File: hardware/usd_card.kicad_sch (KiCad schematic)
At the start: 11 parts, among them J3 MicroSD_502570-0893, U10 AP2112K-3.3, U9 TXB0104D

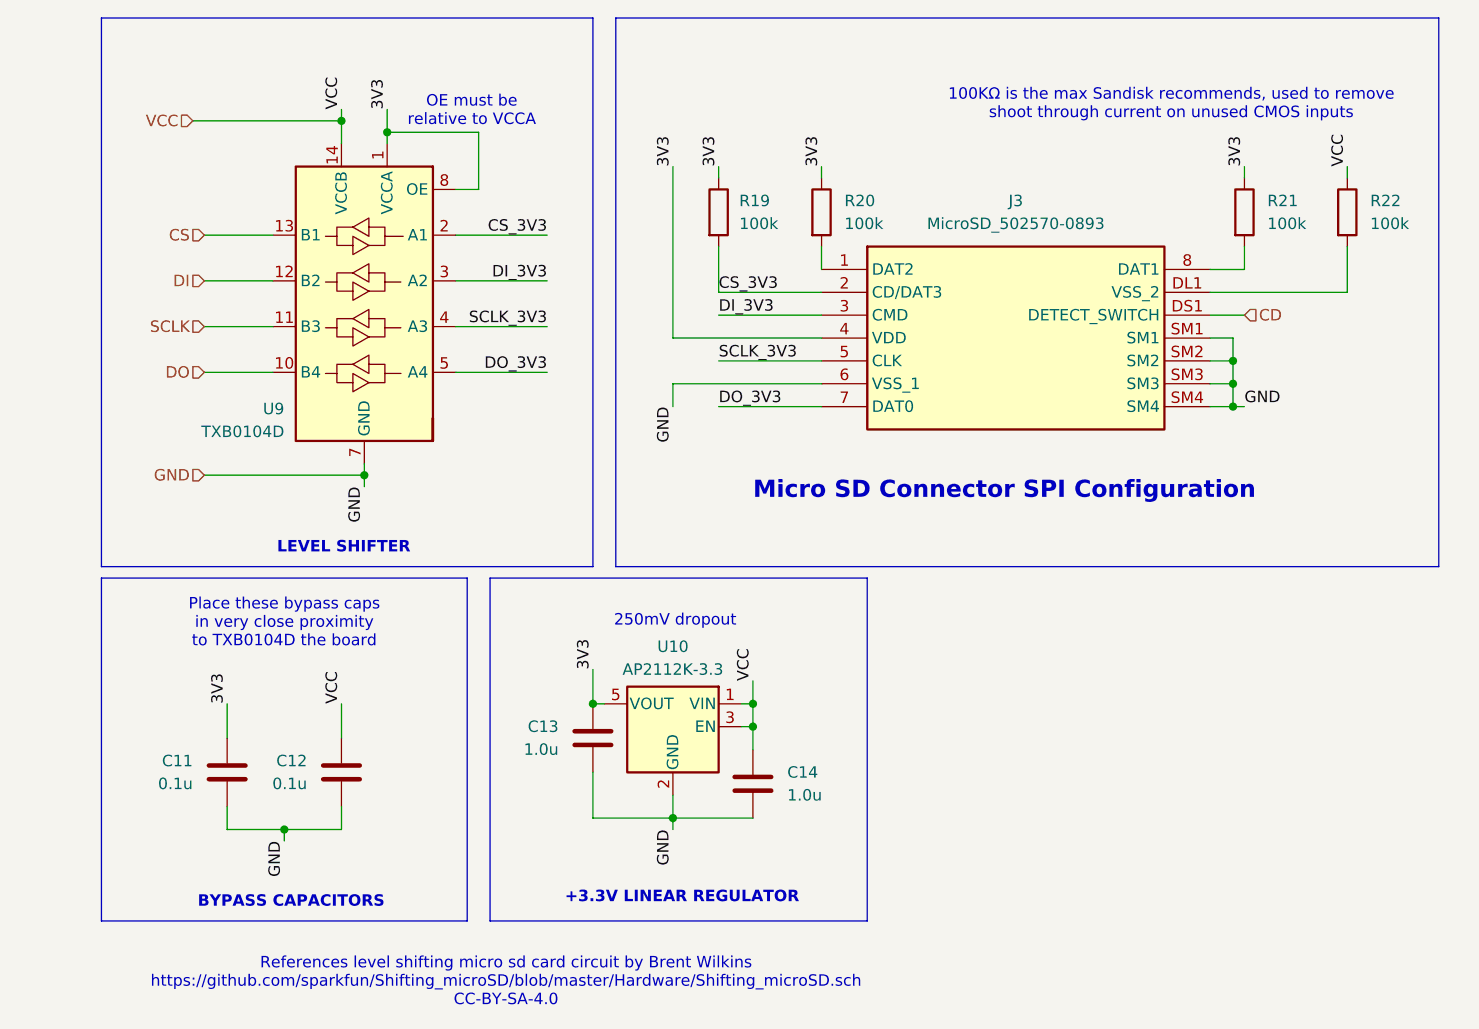
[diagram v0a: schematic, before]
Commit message: organized schem and updated readme
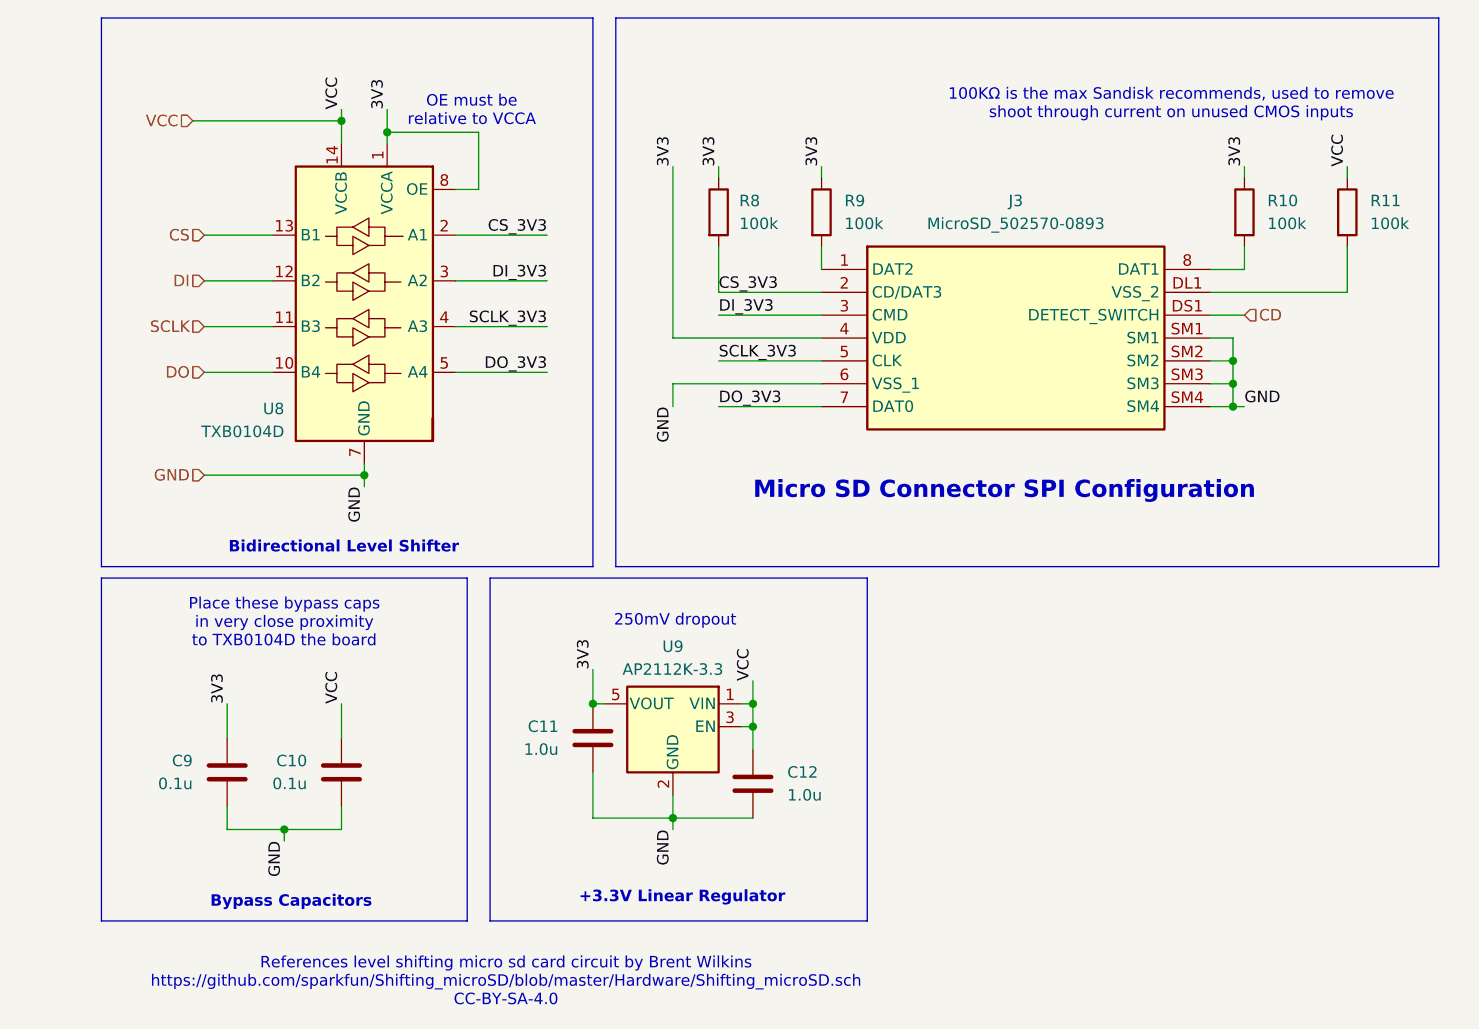
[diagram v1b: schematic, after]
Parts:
- renumbered C12 to C10, C13 to C11, C14 to C12, C11 to C9, R21 to R10, R22 to R11, R19 to R8, R20 to R9, U9 to U8, U10 to U9
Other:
- note added: "+3.3V Linear Regulator"
- note added: "Bidirectional Level Shifter"
- note added: "Bypass Capacitors"
- note removed: "+3.3V LINEAR REGULATOR"
- note removed: "BYPASS CAPACITORS"
- note removed: "LEVEL SHIFTER"
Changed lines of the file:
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@@
 		)
 	)
-	(text "LEVEL SHIFTER"
+	(text "Bidirectional Level Shifter"
 		(exclude_from_sim no)
 		(at 94.234 107.188 0)
@@
 		)
 	)
-	(text "+3.3V LINEAR REGULATOR"
+	(text "+3.3V Linear Regulator"
 		(exclude_from_sim no)
 		(at 131.826 146.05 0)
@@
 		)
 	)
-	(text "BYPASS CAPACITORS"
+	(text "Bypass Capacitors"
 		(exclude_from_sim no)
 		(at 88.392 146.558 0)
@@
 		(on_board yes)
 		(dnp no)
-		(property "Reference" "R20"
+		(property "Reference" "R9"
 			(at 149.86 68.5799 0)
 			(effects
@@
 			(project "BREAD_Slice"
 				(path "/66043bca-a260-4915-9fce-8a51d324c687/2b629e9e-b2ad-4a6d-9037-50f0899b6cc2"
-					(reference "R20")
+					(reference "R9")
 					(unit 1)
 				)
@@
 		(on_board yes)
 		(dnp no)
-		(property "Reference" "C13"
+		(property "Reference" "C11"
 			(at 118.11 126.9999 0)
 			(effects
@@
 			(project "BREAD_Slice"
 				(path "/66043bca-a260-4915-9fce-8a51d324c687/2b629e9e-b2ad-4a6d-9037-50f0899b6cc2"
-					(reference "C13")
+					(reference "C11")
 					(unit 1)
 				)
@@
 		(dnp no)
 		(fields_autoplaced yes)
-		(property "Reference" "R21"
+		(property "Reference" "R10"
 			(at 196.85 68.5799 0)
 			(effects
@@
 			(project "BREAD_Slice"
 				(path "/66043bca-a260-4915-9fce-8a51d324c687/2b629e9e-b2ad-4a6d-9037-50f0899b6cc2"
-					(reference "R21")
+					(reference "R10")
 					(unit 1)
 				)
@@
 		(dnp no)
 		(fields_autoplaced yes)
-		(property "Reference" "R22"
+		(property "Reference" "R11"
 			(at 208.28 68.5799 0)
 			(effects
@@
 			(project "BREAD_Slice"
 				(path "/66043bca-a260-4915-9fce-8a51d324c687/2b629e9e-b2ad-4a6d-9037-50f0899b6cc2"
-					(reference "R22")
+					(reference "R11")
 					(unit 1)
 				)
@@
 		(dnp no)
 		(fields_autoplaced yes)
-		(property "Reference" "U10"
+		(property "Reference" "U9"
 			(at 130.81 118.11 0)
 			(effects
@@
 			(project "BREAD_Slice"
 				(path "/66043bca-a260-4915-9fce-8a51d324c687/2b629e9e-b2ad-4a6d-9037-50f0899b6cc2"
-					(reference "U10")
+					(reference "U9")
 					(unit 1)
 				)
@@
 		(on_board yes)
 		(dnp no)
-		(property "Reference" "R19"
+		(property "Reference" "R8"
 			(at 138.176 68.58 0)
 			(effects
@@
 			(project "BREAD_Slice"
 				(path "/66043bca-a260-4915-9fce-8a51d324c687/2b629e9e-b2ad-4a6d-9037-50f0899b6cc2"
-					(reference "R19")
+					(reference "R8")
 					(unit 1)
 				)
@@
 		(on_board yes)
 		(dnp no)
-		(property "Reference" "C14"
+		(property "Reference" "C12"
 			(at 143.51 132.0799 0)
 			(effects
@@
 			(project "BREAD_Slice"
 				(path "/66043bca-a260-4915-9fce-8a51d324c687/2b629e9e-b2ad-4a6d-9037-50f0899b6cc2"
-					(reference "C14")
+					(reference "C12")
 					(unit 1)
 				)
@@
 		(dnp no)
 		(fields_autoplaced yes)
-		(property "Reference" "C12"
+		(property "Reference" "C10"
 			(at 90.17 130.8099 0)
 			(effects
@@
 			(project "BREAD_Slice"
 				(path "/66043bca-a260-4915-9fce-8a51d324c687/2b629e9e-b2ad-4a6d-9037-50f0899b6cc2"
-					(reference "C12")
+					(reference "C10")
 					(unit 1)
 				)
@@
 		(dnp no)
 		(fields_autoplaced yes)
-		(property "Reference" "C11"
+		(property "Reference" "C9"
 			(at 77.47 130.8099 0)
 			(effects
@@
 			(project "BREAD_Slice"
 				(path "/66043bca-a260-4915-9fce-8a51d324c687/2b629e9e-b2ad-4a6d-9037-50f0899b6cc2"
-					(reference "C11")
+					(reference "C9")
 					(unit 1)
 				)
@@
 		(on_board yes)
 		(dnp no)
-		(property "Reference" "U9"
+		(property "Reference" "U8"
 			(at 87.63 91.694 0)
 			(effects
@@
 			(project "BREAD_Slice"
 				(path "/66043bca-a260-4915-9fce-8a51d324c687/2b629e9e-b2ad-4a6d-9037-50f0899b6cc2"
-					(reference "U9")
+					(reference "U8")
 					(unit 1)
 				)

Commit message: completed board
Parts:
- C10, C11, C12, C9: footprint (none) -> Capacitor_SMD:C_1206_3216Metric_Pad1.33x1.80mm_HandSolder
- J3: footprint 5025700893 -> KML-Custom:MicroSD_5025700893
- R11: renamed from R8; footprint (none) -> Resistor_SMD:R_1206_3216Metric_Pad1.30x1.75mm_HandSolder
- R12: renamed from R9; footprint (none) -> Resistor_SMD:R_1206_3216Metric_Pad1.30x1.75mm_HandSolder
- R13: renamed from R10; footprint (none) -> Resistor_SMD:R_1206_3216Metric_Pad1.30x1.75mm_HandSolder
- R14: renamed from R11; footprint (none) -> Resistor_SMD:R_1206_3216Metric_Pad1.30x1.75mm_HandSolder
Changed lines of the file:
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@@
 		(on_board yes)
 		(dnp no)
-		(property "Reference" "R9"
+		(property "Reference" "R12"
 			(at 149.86 68.5799 0)
 			(effects
@@
 			)
 		)
-		(property "Footprint" ""
+		(property "Footprint" "Resistor_SMD:R_1206_3216Metric_Pad1.30x1.75mm_HandSolder"
 			(at 145.542 69.85 90)
 			(effects
@@
 			(project "BREAD_Slice"
 				(path "/66043bca-a260-4915-9fce-8a51d324c687/2b629e9e-b2ad-4a6d-9037-50f0899b6cc2"
-					(reference "R9")
+					(reference "R12")
 					(unit 1)
 				)
@@
 			)
 		)
-		(property "Footprint" ""
+		(property "Footprint" "Capacitor_SMD:C_1206_3216Metric_Pad1.33x1.80mm_HandSolder"
 			(at 120.9548 132.08 0)
 			(effects
@@
 		(dnp no)
 		(fields_autoplaced yes)
-		(property "Reference" "R10"
+		(property "Reference" "R13"
 			(at 196.85 68.5799 0)
 			(effects
@@
 			)
 		)
-		(property "Footprint" ""
+		(property "Footprint" "Resistor_SMD:R_1206_3216Metric_Pad1.30x1.75mm_HandSolder"
 			(at 192.532 69.85 90)
 			(effects
@@
 			(project "BREAD_Slice"
 				(path "/66043bca-a260-4915-9fce-8a51d324c687/2b629e9e-b2ad-4a6d-9037-50f0899b6cc2"
-					(reference "R10")
+					(reference "R13")
 					(unit 1)
 				)
@@
 		(dnp no)
 		(fields_autoplaced yes)
-		(property "Reference" "R11"
+		(property "Reference" "R14"
 			(at 208.28 68.5799 0)
 			(effects
@@
 			)
 		)
-		(property "Footprint" ""
+		(property "Footprint" "Resistor_SMD:R_1206_3216Metric_Pad1.30x1.75mm_HandSolder"
 			(at 203.962 69.85 90)
 			(effects
@@
 			(project "BREAD_Slice"
 				(path "/66043bca-a260-4915-9fce-8a51d324c687/2b629e9e-b2ad-4a6d-9037-50f0899b6cc2"
-					(reference "R11")
+					(reference "R14")
 					(unit 1)
 				)
@@
 		(on_board yes)
 		(dnp no)
-		(property "Reference" "R8"
+		(property "Reference" "R11"
 			(at 138.176 68.58 0)
 			(effects
@@
 			)
 		)
-		(property "Footprint" ""
+		(property "Footprint" "Resistor_SMD:R_1206_3216Metric_Pad1.30x1.75mm_HandSolder"
 			(at 134.112 69.85 90)
 			(effects
@@
 			(project "BREAD_Slice"
 				(path "/66043bca-a260-4915-9fce-8a51d324c687/2b629e9e-b2ad-4a6d-9037-50f0899b6cc2"
-					(reference "R8")
+					(reference "R11")
 					(unit 1)
 				)
@@
 			)
 		)
-		(property "Footprint" ""
+		(property "Footprint" "Capacitor_SMD:C_1206_3216Metric_Pad1.33x1.80mm_HandSolder"
 			(at 140.6652 137.16 0)
 			(effects
@@
 			)
 		)
-		(property "Footprint" ""
+		(property "Footprint" "Capacitor_SMD:C_1206_3216Metric_Pad1.33x1.80mm_HandSolder"
 			(at 93.0148 135.89 0)
 			(effects
@@
 			)
 		)
-		(property "Footprint" ""
+		(property "Footprint" "Capacitor_SMD:C_1206_3216Metric_Pad1.33x1.80mm_HandSolder"
 			(at 80.3148 135.89 0)
 			(effects
@@
 			)
 		)
-		(property "Footprint" "5025700893"
+		(property "Footprint" "KML-Custom:MicroSD_5025700893"
 			(at 186.69 171.12 0)
 			(effects
